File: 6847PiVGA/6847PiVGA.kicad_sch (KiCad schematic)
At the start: 44 parts, among them J1 DB15_Female_HighDensity, J2 Conn_01x06_Male, U1 MC6847, U2 AD724JRZ, U3 Pico, U4 AD813, U5 TXS0108EPW, U6 2N7001T, U7 TXS0108EPW, Y1 4.433620MHz

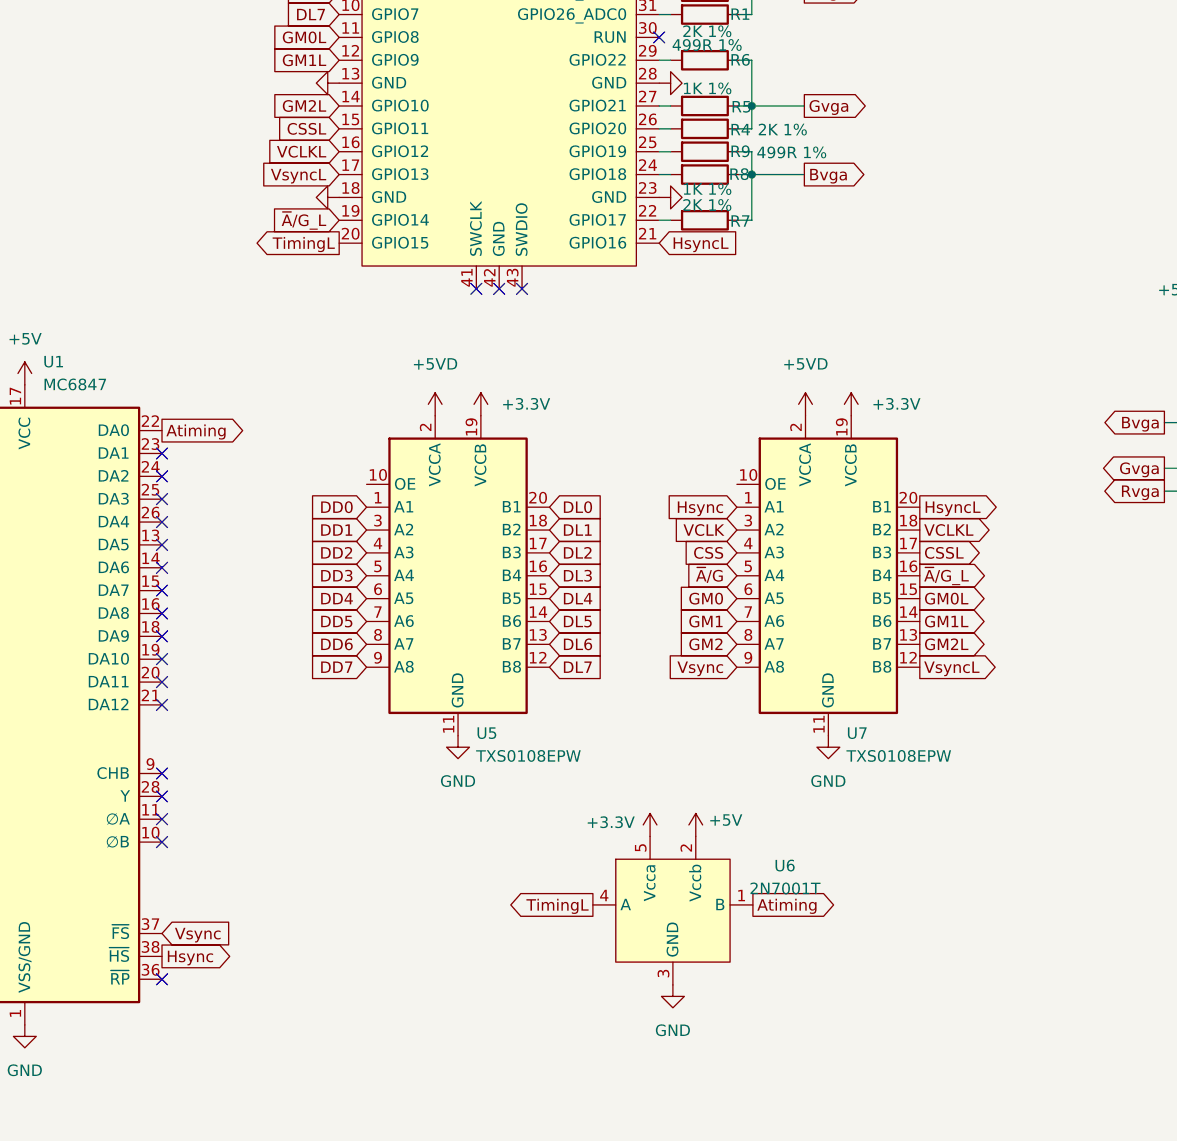
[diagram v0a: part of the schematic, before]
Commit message: switch synclines from input to output
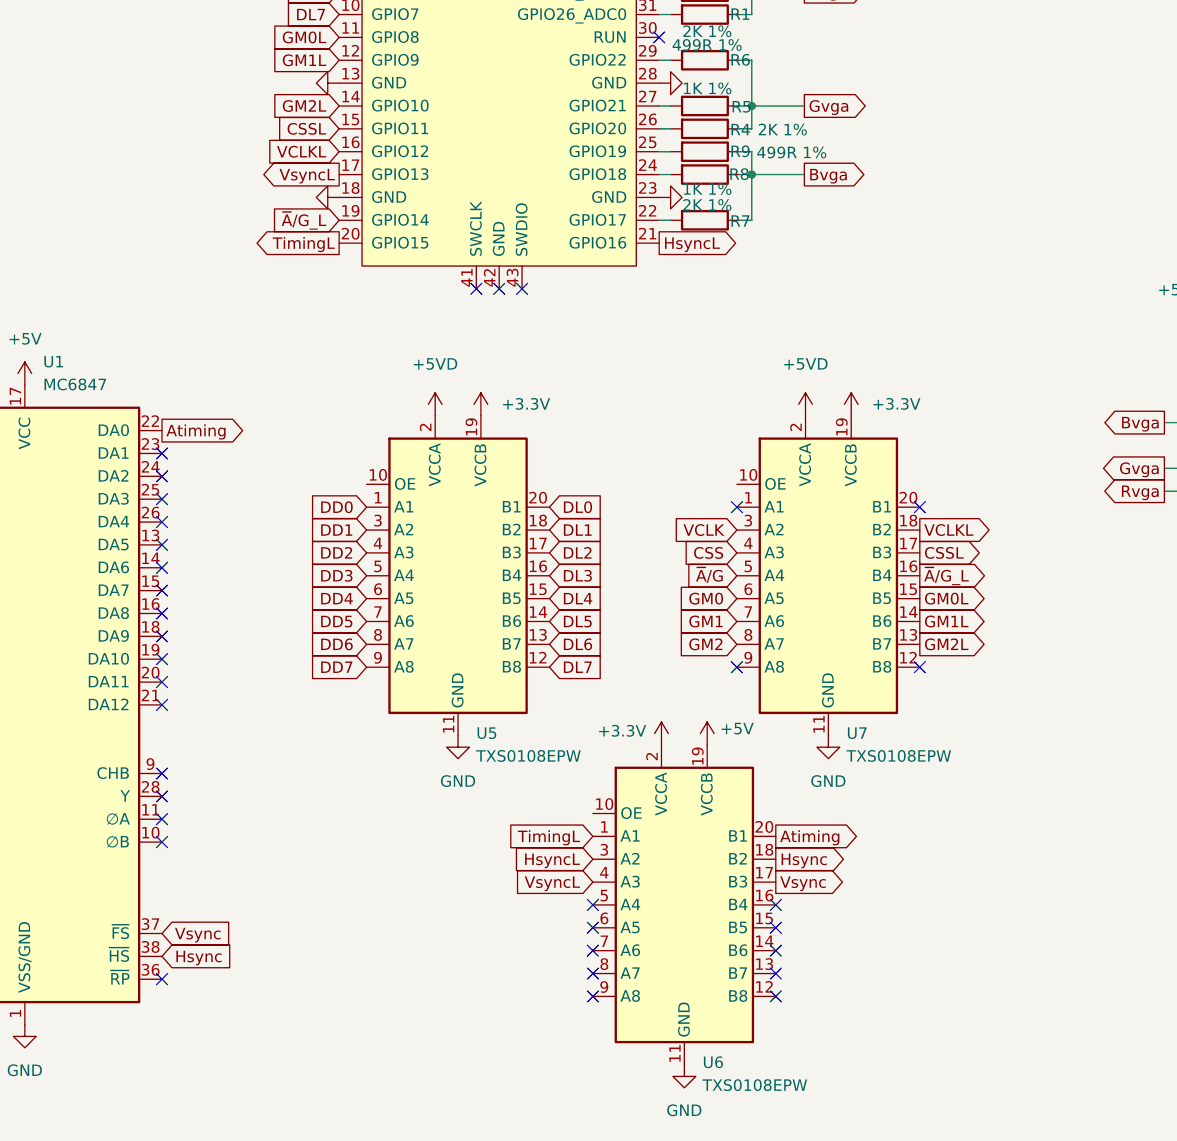
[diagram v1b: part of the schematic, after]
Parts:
- removed U6: 2N7001T, Package_TO_SOT_SMD:SOT-353_SC-70-5, symbol 6847P:2N7001T
- added U6: TXS0108EPW, Package_SO:TSSOP-20_4.4x6.5mm_P0.65mm, symbol Logic_LevelTranslator:TXS0108EPW
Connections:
- net +3.3V: now also U6.2 (VCCA)
- net +5V: now also U6.19 (VCCB)
- net Atiming: now also U6.20 (B1)
- net GND: now also U6.11 (GND)
- net Hsync: now also U6.18 (B2); no longer U7.1 (A1)
- net HsyncL: now also U6.3 (A2); no longer U7.20 (B1)
- net TimingL: now also U6.1 (A1)
- net Vsync: now also U6.17 (B3); no longer U7.9 (A8)
- net VsyncL: now also U6.4 (A3); no longer U7.12 (B8)
- no-connect marks 30 -> 44

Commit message: tidyup
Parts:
- added C12, C13, C14, C15, C16, C17: 100nF, Capacitor_SMD:C_0805_2012Metric, symbol Device:C
- added R23: 4K7, Resistor_SMD:R_0805_2012Metric, symbol Device:R
- C4, C6: footprint Capacitor_SMD:C_0805_2012Metric -> Capacitor_SMD:C_1206_3216Metric_Pad1.33x1.80mm_HandSolder
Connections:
- net +3.3V: now also U5.10 (OE), U5.2 (VCCA), U6.10 (OE), U7.10 (OE), U7.2 (VCCA), C12.1, C13.1, C15.1, R23.1; no longer U5.19 (VCCB), U7.19 (VCCB)
- net +5V: no longer U6.19 (VCCB)
- net +5VD: now also U5.19 (VCCB), U6.19 (VCCB), U7.19 (VCCB), C14.1, C16.1, C17.1; no longer U5.2 (VCCA), U7.2 (VCCA)
- net CSS: now also U7.18 (B2); no longer U7.4 (A3)
- net CSSL: now also U7.3 (A2); no longer U7.17 (B3)
- net DD0: now also U5.20 (B1); no longer U5.1 (A1)
- net DD1: now also U5.18 (B2); no longer U5.3 (A2)
- net DD2: now also U5.17 (B3); no longer U5.4 (A3)
- net DD3: now also U5.16 (B4); no longer U5.5 (A4)
- net DD4: now also U5.15 (B5); no longer U5.6 (A5)
- net DD5: now also U5.14 (B6); no longer U5.7 (A6)
- net DD6: now also U5.13 (B7); no longer U5.8 (A7)
- net DD7: now also U5.12 (B8); no longer U5.9 (A8)
- net DL0: now also U5.1 (A1); no longer U5.20 (B1)
- net DL1: now also U5.3 (A2); no longer U5.18 (B2)
- net DL2: now also U5.4 (A3); no longer U5.17 (B3)
- net DL3: now also U5.5 (A4); no longer U5.16 (B4)
- net DL4: now also U5.6 (A5); no longer U5.15 (B5)
- net DL5: now also U5.7 (A6); no longer U5.14 (B6)
- net DL6: now also U5.8 (A7); no longer U5.13 (B7)
- net DL7: now also U5.9 (A8); no longer U5.12 (B8)
- net GM0: now also U7.15 (B5); no longer U7.6 (A5)
- net GM0L: now also U7.6 (A5); no longer U7.15 (B5)
- net GM1: now also U7.14 (B6); no longer U7.7 (A6)
- net GM1L: now also U7.7 (A6); no longer U7.14 (B6)
- net GM2: now also U7.13 (B7); no longer U7.8 (A7)
- net GM2L: now also U7.8 (A7); no longer U7.13 (B7)
- net GND: now also J1.0 (Shield), C12.2, C13.2, C14.2, C15.2, C16.2, C17.2, R23.2
- net HsyncL: now also U3.20 (GPIO15); no longer U3.21 (GPIO16)
- net TimingL: now also U3.21 (GPIO16); no longer U3.20 (GPIO15)
- net VCLK: now also U7.17 (B3); no longer U7.3 (A2)
- net VCLKL: now also U7.4 (A3); no longer U7.18 (B2)
- net ~{A}/G: now also U7.16 (B4); no longer U7.5 (A4)
- net ~{A}/G_L: now also U7.5 (A4); no longer U7.16 (B4)
- no-connect marks 44 -> 46
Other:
- moved on the sheet: C11, D1, R1, R2, R3, R4, R5, R6, R7, R8, R9, U5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
